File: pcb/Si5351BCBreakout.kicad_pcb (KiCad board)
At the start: 2 copper layers, 42 x 60 mm, 47 parts, among them J1 Power/IO, J10 CLK4, J11 CLK0, J12 CLK2, J2 VC/CLKIN, J3 VC/CLKIN, J4 PS Sel, J5 3.3V Sel, J6 CLK3-CLK7, J7 CLK4, J8 CLK0, J9 CLK2, Q1 2N7002, Q2 2N7002, U1 LP2985-3.3, U2 ASTX-H11-25.000MHZ-T, U3 Si5351B/C

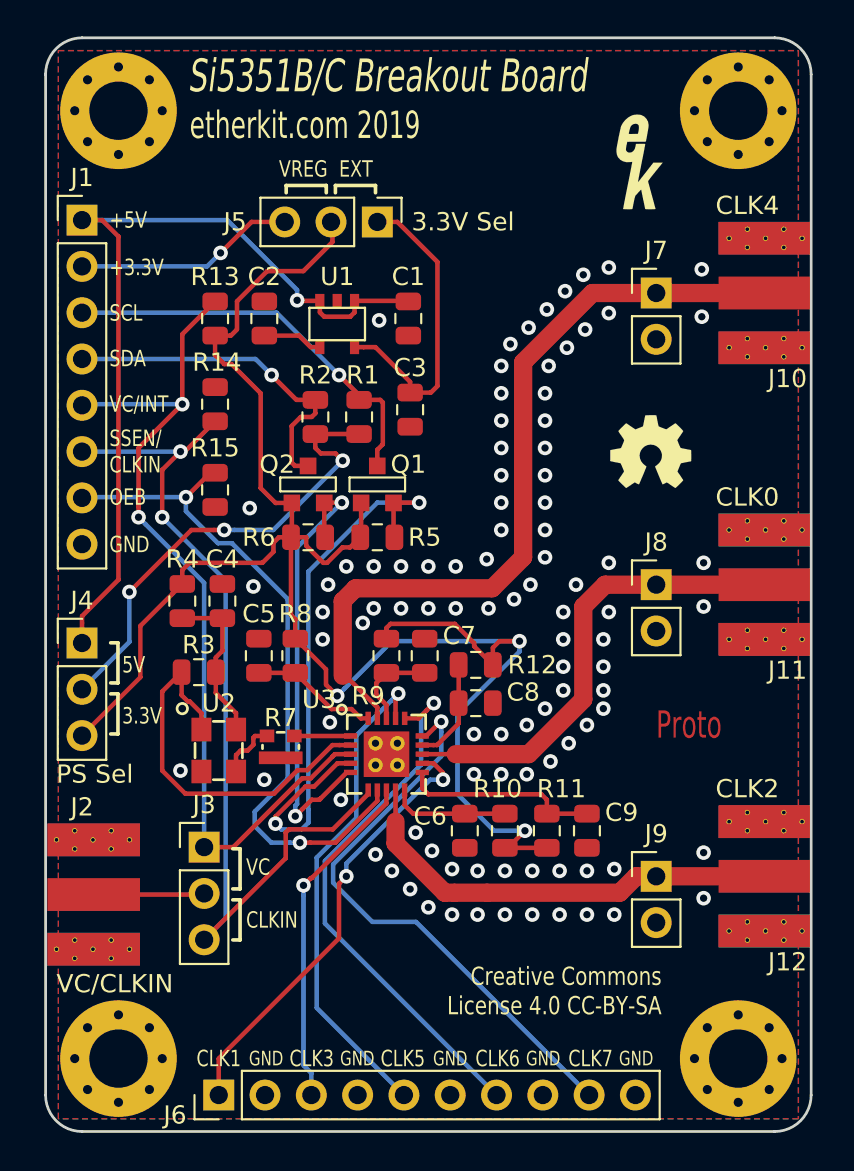
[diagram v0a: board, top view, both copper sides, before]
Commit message: First pass of Rev B. Change to 4 layers
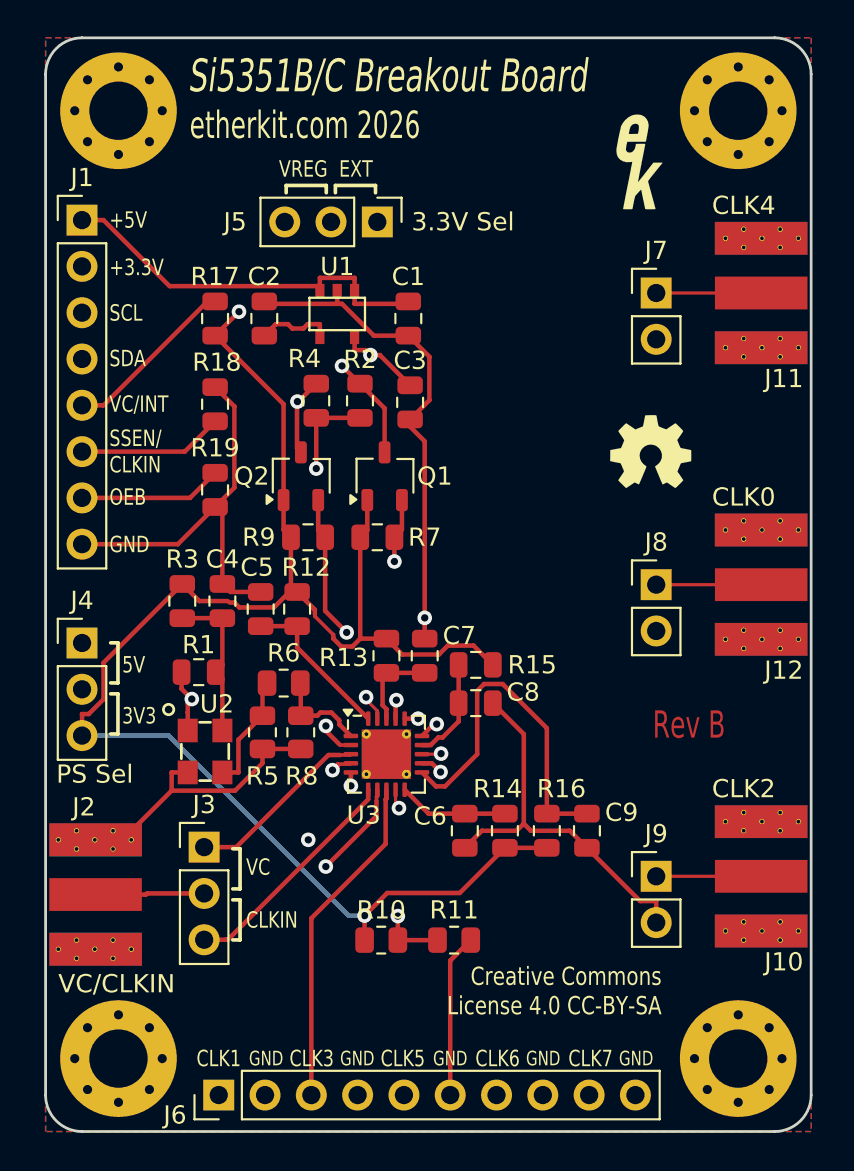
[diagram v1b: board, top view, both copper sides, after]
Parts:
- removed the R7 at (112.9, 88.9)
- removed REF** (x4): MountingHole_3.2mm_M3_Pad_Via, MountingHole:MountingHole_3.2mm_M3_Pad_Via
- added H1: MountingHole_Pad, MountingHole:MountingHole_3.2mm_M3_Pad_Via, F.Cu at (104.0, 54.0)
- added H2: MountingHole_Pad, MountingHole:MountingHole_3.2mm_M3_Pad_Via, F.Cu at (138.0, 54.0)
- added H3: MountingHole_Pad, MountingHole:MountingHole_3.2mm_M3_Pad_Via, F.Cu at (104.0, 106.0)
- added H4: MountingHole_Pad, MountingHole:MountingHole_3.2mm_M3_Pad_Via, F.Cu at (138.0, 106.0)
- added R10: 10k, Resistor_SMD:R_0805_2012Metric, F.Cu at (118.4, 99.5)
- added R11: 10k, Resistor_SMD:R_0805_2012Metric, F.Cu at (122.4, 99.5)
- added R5: 300, Resistor_SMD:R_0805_2012Metric, F.Cu at (111.9, 88.1)
- added R6: 18, Resistor_SMD:R_0805_2012Metric, F.Cu at (113.1, 85.4)
- added R8: 300, Resistor_SMD:R_0805_2012Metric, F.Cu at (114.0, 88.1)
- C2: value 100n -> 10n
- Q1, Q2: value 2N7002 -> BSS138; footprint EtherkitKicadLibrary:SOT23-2N7002 -> Package_TO_SOT_SMD:TSOT-23
- U3: footprint EtherkitKicadLibrary:QFN-20-1EP_4x4mm_Pitch0.5mm -> Package_DFN_QFN:QFN-20-1EP_4x4mm_P0.5mm_EP2.7x2.7mm_ThermalVias
- moved C5 2.56 mm to (111.8, 81.3)
- moved R12 2.56 mm to (113.8, 81.3)
- moved R2 0.89 mm to (117.2, 69.9)
- moved R4 0.89 mm to (114.8, 69.9)
- moved U2 0.75 mm to (108.8, 89.2)
- moved Q1 0.60 mm to (118.6, 74.0), turned to 90 degrees
- moved Q2 0.60 mm to (114.0, 74.0), turned to 90 degrees
- moved U1 0.55 mm to (116.0, 65.2)
- moved C3 0.40 mm to (120.0, 70.0)
- moved J10 0.20 mm to (141.8, 96.0)
- moved J11 0.20 mm to (141.8, 64.0)
- moved J12 0.20 mm to (141.8, 80.0)
- moved J2 0.10 mm to (100.2, 97.0)
- renumbered J12 to J10, J10 to J11, J11 to J12, R3 to R1, R8 to R12, R9 to R13, R10 to R14, R12 to R15, R11 to R16, R13 to R17, R14 to R18, R15 to R19, R1 to R2, R4 to R3, R2 to R4, R5 to R7, R6 to R9
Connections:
- Q1 pad 1: Net-(Q1-Pad1) -> +3.3VREG
- Q1 pad 2: +3.3VREG -> Net-(Q1-S)
- Q2 pad 1: Net-(Q2-Pad1) -> +3.3VREG
- Q2 pad 2: +3.3VREG -> Net-(Q2-S)
- R7 pad 2: Net-(Q1-Pad1) -> Net-(Q1-S)
- R9 pad 2: Net-(Q2-Pad1) -> Net-(Q2-S)
- U3 pad 4: Net-(Q1-Pad1) -> Net-(Q1-S)
- U3 pad 5: Net-(Q2-Pad1) -> Net-(Q2-S)
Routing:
- net GND: track 0.00 -> 272.4 mm, vias 95 -> 1
- net Net-(Q1-Pad1): track 32.6 -> 0.00 mm, vias 2 -> 0
- net Net-(Q2-Pad1): track 25.3 -> 0.00 mm, vias 2 -> 0
- net Net-(Q1-S): track 0.00 -> 18.0 mm, vias 0 -> 2
- net Net-(Q2-S): track 0.00 -> 17.3 mm, vias 0 -> 2
- net VC_INTR: track 48.8 -> 62.9 mm, vias 2 -> 1
- net OEB: track 38.1 -> 47.8 mm, vias 2 -> 1
- net Net-(U3-VDDOA): track 10.9 -> 19.4 mm
- net Net-(U2-OE): track 21.5 -> 13.5 mm, vias 0 -> 2
- net CLK4: track 43.8 -> 36.3 mm, vias 0 -> 1
- net CLK6: track 29.8 -> 23.2 mm
- net CLK7: track 31.5 -> 24.9 mm
- net Net-(J5-Pin_1): track 17.1 -> 12.0 mm, vias 0 -> 1
- net CLK5: track 27.3 -> 23.5 mm
- net Net-(U2-OUT): track 3.26 -> 6.43 mm
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- added copper zone on In2.Cu, net +3.3VREG
- added copper zone on In1.Cu, net GND
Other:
- copper layers 2 -> 4
- net class 50 Ohm removed
- net class Default removed
- board text added: "3V3"
- board text added: "Rev B"
- board text added: "etherkit.com 2026"
- board text removed: "3.3V"
- board text removed: "Proto"
- board text removed: "etherkit.com 2019"

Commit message: TCXO change
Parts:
- removed R17: 10k, Resistor_SMD:R_0805_2012Metric
- added R20: 0, Resistor_SMD:R_0805_2012Metric, F.Cu at (124.9, 89.8)
- added R21: 0, Resistor_SMD:R_0805_2012Metric, F.Cu at (120.0, 94.5)
- added R22: 0, Resistor_SMD:R_0805_2012Metric, F.Cu at (123.5, 82.1)
- moved C9 13.2 mm to (120.7, 83.9)
- moved C5 3.73 mm to (112.9, 84.9), turned to 180 degrees
- moved R5 2.90 mm to (111.9, 91.0)
- moved R8 2.90 mm to (114.0, 91.0)
- moved R6 2.90 mm to (113.1, 88.3)
- moved C7 2.17 mm to (118.6, 83.9)
- moved R13 2.17 mm to (116.5, 83.9)
- moved C8 1.99 mm to (125.6, 86.8)
- moved R15 1.99 mm to (125.6, 84.7)
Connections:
- J10 pad 1: CLK2 -> /CLK2_OUT
- J11 pad 1: CLK4 -> /CLK4_OUT
- J12 pad 1: CLK0 -> /CLK0_OUT
- J7 pad 1: CLK4 -> /CLK4_OUT
- J8 pad 1: CLK0 -> /CLK0_OUT
- J9 pad 1: CLK2 -> /CLK2_OUT
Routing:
- net /CLK4_OUT: track 0.00 -> 30.1 mm, vias 0 -> 1
- net GND: track 272.4 -> 246.3 mm, vias 1 -> 0
- net CLK4: track 36.3 -> 11.3 mm, vias 1 -> 2
- net /CLK0_OUT: track 0.00 -> 23.2 mm, vias 0 -> 1
- net /CLK2_OUT: track 0.00 -> 22.2 mm, vias 0 -> 1
- net CLK2: track 22.7 -> 2.62 mm, vias 1 -> 0
- net CLK0: track 22.7 -> 4.51 mm, vias 1 -> 0
- net +3.3VREG: track 97.2 -> 85.8 mm, vias 2 -> 3
- net VC_INTR: track 62.9 -> 55.3 mm
- net CLK7: track 24.9 -> 30.2 mm
- net OEB: track 47.8 -> 43.5 mm
- net Net-(U2-OE): track 13.5 -> 16.9 mm, vias 2 -> 0
- net Net-(Q1-S): track 18.0 -> 21.0 mm
- net Net-(U2-OUT): track 6.43 -> 4.16 mm
- net CLK1: track 26.1 -> 24.2 mm, vias 2 -> 1
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
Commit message: Add logos to PCB
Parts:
- moved Ref** 16.6 mm to (127.8, 72.7)
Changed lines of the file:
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@@
 	(footprint "EtherkitKicadLibrary:EtherkitLogoSmall"
 		(layer "F.Cu")
-		(at 132.6 56.8)
+		(at 127.8 72.7)
 		(property "Reference" "Ref**"
 			(at 0 3.25 0)
@@
 		)
 		(min_thickness 0.25)
-		(fill
+		(fill yes
 			(thermal_gap 0.25)
 			(thermal_bridge_width 0.3)
@@
 		)
 		(min_thickness 0.25)
-		(fill
+		(fill yes
 			(thermal_gap 0.25)
 			(thermal_bridge_width 0.3)
@@
 		)
 		(min_thickness 0.25)
-		(fill
+		(fill yes
 			(thermal_gap 0.5)
 			(thermal_bridge_width 0.5)
@@
 		)
 		(min_thickness 0.25)
-		(fill
+		(fill yes
 			(thermal_gap 0.5)
 			(thermal_bridge_width 0.5)
